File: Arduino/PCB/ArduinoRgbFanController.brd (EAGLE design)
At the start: 100 x 100 mm, 58 parts, among them IC2 ARDUINO_MKRFOX1200PROTOPADS, Q1 IRLML9301TRPBF, Q2 2N7002, Q3 2N7002, Q4 IRLML9301TRPBF

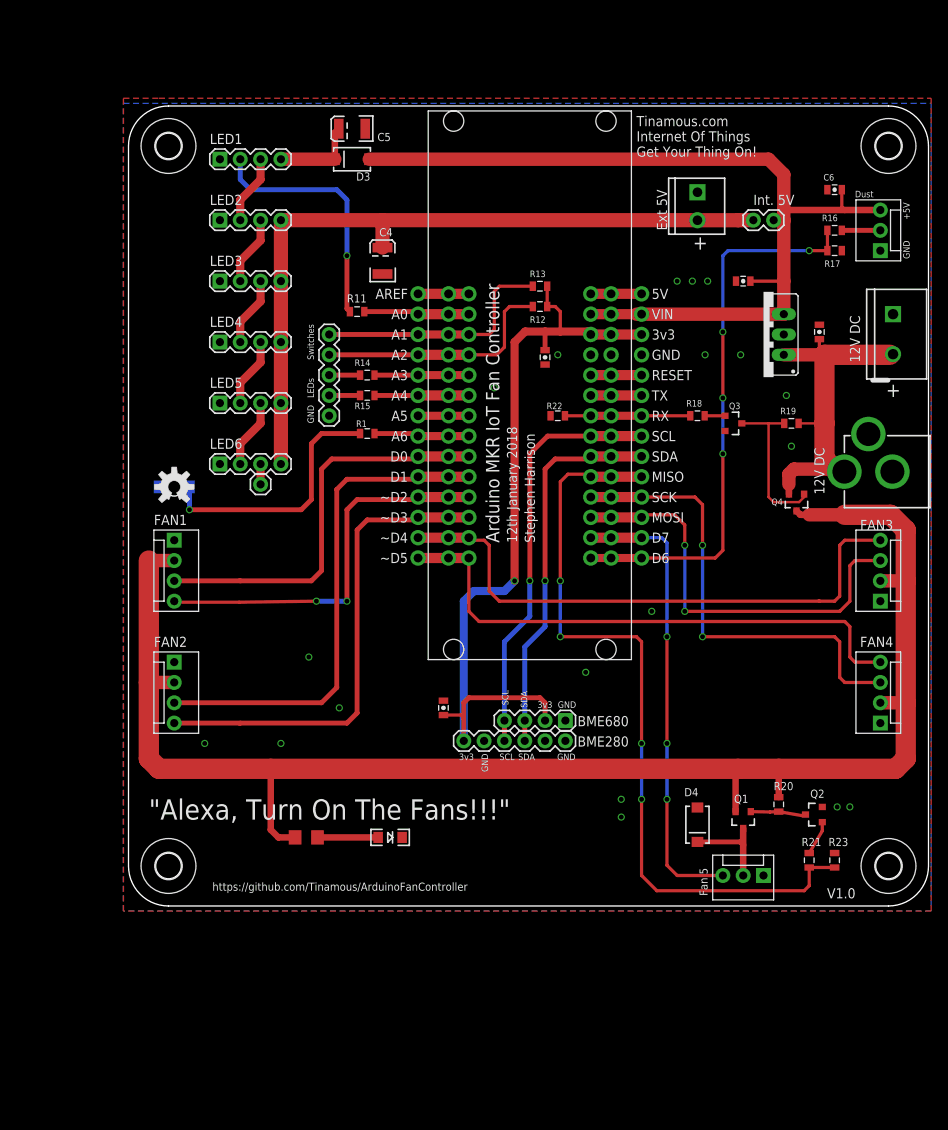
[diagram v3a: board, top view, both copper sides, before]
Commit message: Added 12v sense to detect low voltage and supply switched on.
Moved Fan5 connector up to leave a nice space at the bottom for the "Alexa..." thing.
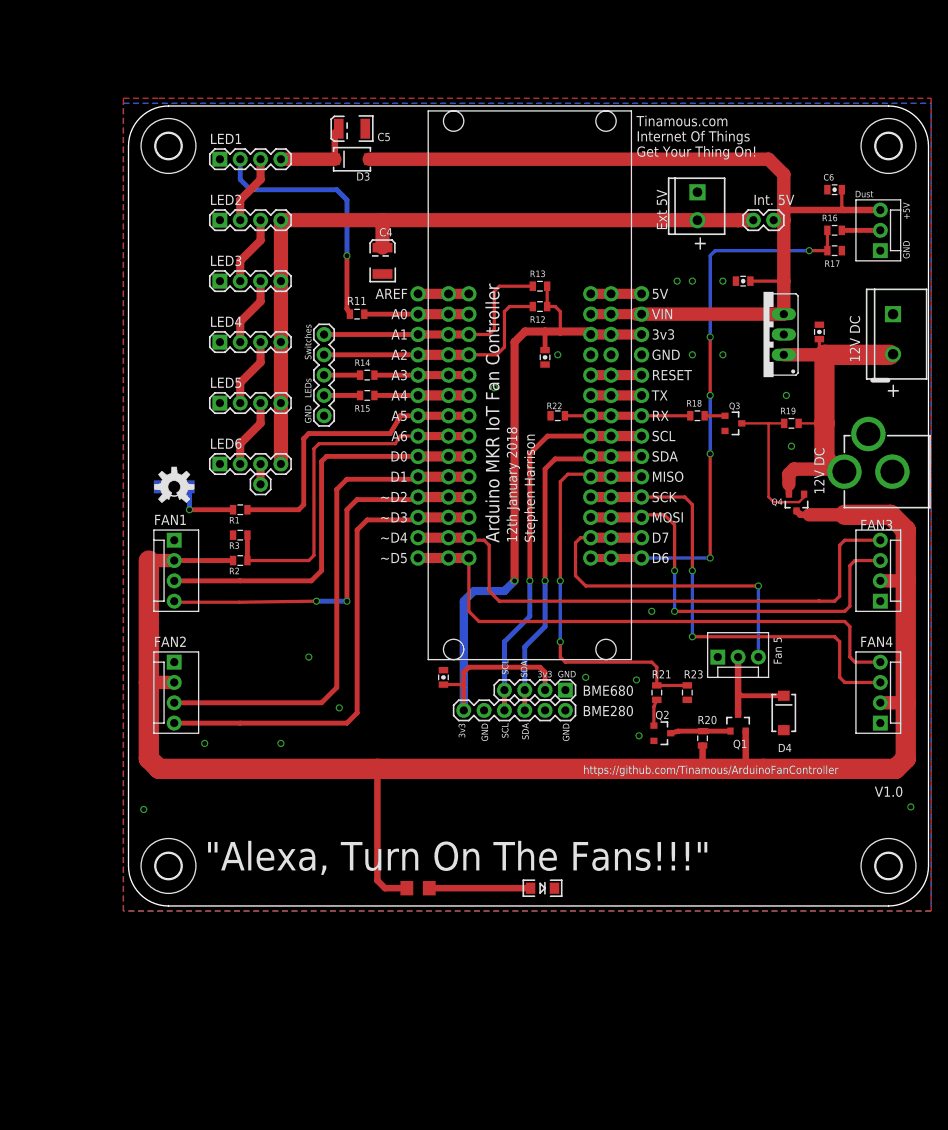
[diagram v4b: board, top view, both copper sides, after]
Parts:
- added R2: 40k, SparkFun-Resistors:0805
- added R3: 10k, SparkFun-Resistors:0805
- moved R21 28.3 mm to (66.0, 26.7), turned to 90 degrees
- moved R23 27.9 mm to (69.8, 26.7), turned to 270 degrees
- moved JP35 27.9 mm to (73.7, 31.1), turned to 0 degrees
- moved Q2 21.6 mm to (66.7, 21.6), turned to 270 degrees
- moved D2 20.1 mm to (51.8, 2.22)
- moved R1 18.5 mm to (14.0, 49.5)
- moved D4 17.7 mm to (81.9, 24.1), turned to 90 degrees
- moved R28 15.3 mm to (36.2, 2.22)
- moved R20 12.6 mm to (71.8, 21.0), turned to 270 degrees
- moved Q1 12.1 mm to (76.2, 22.9), turned to 0 degrees
- moved BME280 3.81 mm to (41.9, 24.4)
- moved BME680 3.81 mm to (54.6, 27.0)
- moved C7 3.81 mm to (39.4, 28.6)
- moved JP3 0.63 mm to (24.4, 61.3)
- moved R11 0.32 mm to (28.6, 74.0)
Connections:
- removed net SWITCH_ENABLED: IC2.#A5, IC2.@A5, IC2.A5
- new net FAN_POWER_SENSE: IC2.#A6, IC2.@A6, IC2.A6, R2.2, R3.1
- net FAN_POWER: now also R2.1
- net GND: now also R3.2
- net OSH_LED: now also IC2.#A5, IC2.@A5, IC2.A5; no longer IC2.#A6, IC2.@A6, IC2.A6
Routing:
- net FAN5_PWM: track 97.1 -> 51.3 mm, vias 4 -> 2
- net FAN_POWER_SENSE: track 0.00 -> 45.2 mm
- net OSH_LED: track 11.9 -> 37.7 mm
- net N$1: track 32.3 -> 8.35 mm
- net FAN_POWER: track 196.4 -> 211.3 mm
- net FAN5_TACH: track 57.6 -> 44.9 mm, vias 3 -> 1
- net SWITCH_ENABLED: track 6.35 -> 0.00 mm
- net N$94: track 7.58 -> 12.7 mm
- net SDA: track 47.7 -> 43.9 mm
- net SCL: track 52.1 -> 48.3 mm
- net 3.3V: track 101.4 -> 97.6 mm
- net N$28: track 6.90 -> 10.4 mm
- net N$12: track 11.8 -> 13.0 mm
- net N$32: track 4.31 -> 3.30 mm
- net SWITCH2: track 30.7 -> 31.4 mm
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
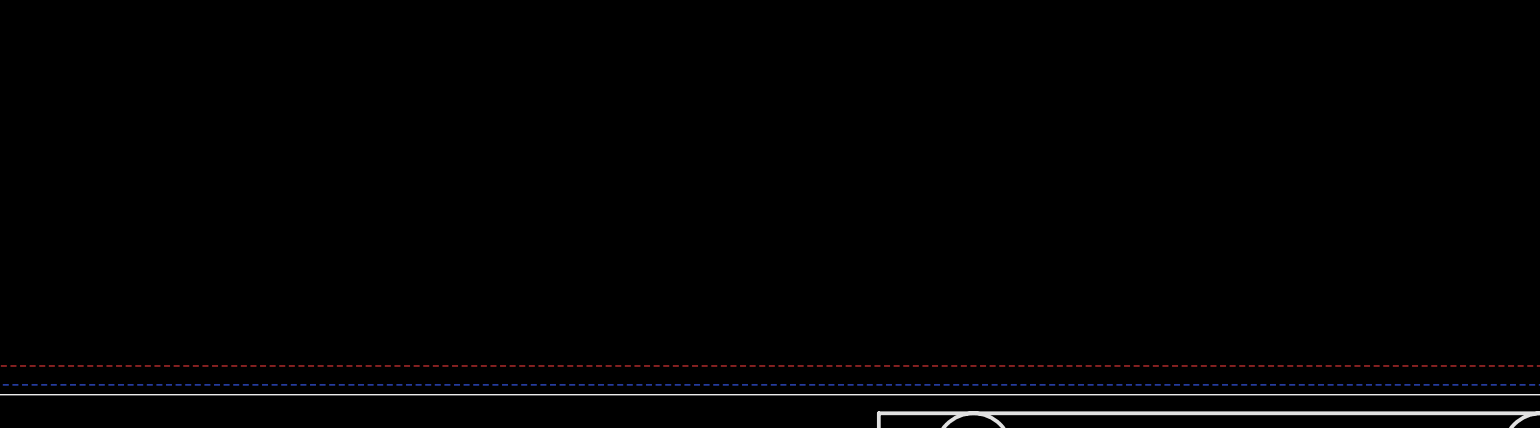
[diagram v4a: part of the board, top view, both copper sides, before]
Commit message: Added some value for components and some notes and dimensions for the PCB.
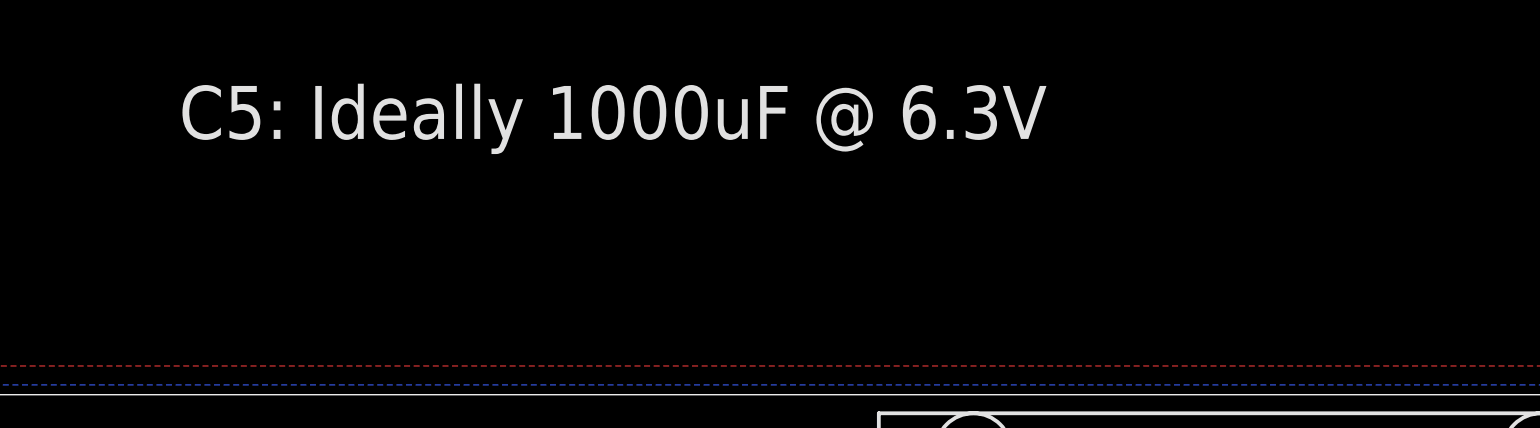
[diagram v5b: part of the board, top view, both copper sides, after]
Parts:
- R11: value (none) -> 470R
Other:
- board text added: "C5: Ideally 1000uF @ 6.3V"
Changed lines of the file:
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@@
 <setting verticaltext="up"/>
 </settings>
-<grid distance="0.025" unitdist="inch" unit="inch" style="lines" multiple="1" display="no" altdistance="0.0125" altunitdist="inch" altunit="inch"/>
+<grid distance="0.1" unitdist="mm" unit="mm" style="lines" multiple="1" display="no" altdistance="0.0125" altunitdist="inch" altunit="inch"/>
 <layers>
 <layer number="1" name="Top" color="4" fill="1" visible="yes" active="yes"/>
@@
 <text x="90.17" y="4.445" size="3.556" layer="26" ratio="15" rot="MR0">"Alexa, Turn On The Fans!!!"</text>
 <text x="72.39" y="83.82" size="1.778" layer="25" font="vector" ratio="10" rot="R180">+</text>
+<dimension x1="95" y1="0" x2="93.98" y2="25.4" x3="108.585" y3="12.7" textsize="1.778" layer="20" dtype="vertical"/>
+<dimension x1="95" y1="0" x2="93.98" y2="40.64" x3="114.3" y3="20.32" textsize="1.778" layer="20" dtype="vertical"/>
+<dimension x1="95" y1="0" x2="103.1875" y2="54.2925" x3="119.38" y3="27.14625" textsize="1.778" layer="20" dtype="vertical"/>
+<dimension x1="95" y1="0" x2="97.155" y2="69.85" x3="127" y3="34.925" textsize="1.778" layer="20" dtype="vertical"/>
+<dimension x1="94.9325" y1="65.7225" x2="96.52" y2="77.47" x3="111.125" y3="71.59625" textsize="1.778" layer="20" dtype="vertical"/>
+<dimension x1="95" y1="0" x2="60.325" y2="61.2775" x3="123.19" y3="30.63875" textsize="1.778" layer="20" dtype="vertical"/>
+<text x="13.97" y="108.585" size="1.778" layer="25">C5: Ideally 1000uF @ 6.3V</text>
+<dimension x1="93.98" y1="81.915" x2="95.25" y2="0" x3="135.89" y3="40.9575" textsize="1.778" layer="47" dtype="vertical"/>
+<dimension x1="40.005" y1="76.5175" x2="5" y2="95" x3="-6.5" y3="85.75875" textsize="1.778" layer="47" dtype="vertical"/>
+<dimension x1="40.005" y1="76.5175" x2="40.4" y2="100" x3="-11.2" y3="88.25875" textsize="1.778" layer="47" dtype="vertical"/>
+<dimension x1="40.005" y1="76.5175" x2="0" y2="74.1" x3="20.0025" y3="114.1" textsize="1.778" layer="47" dtype="horizontal"/>
 </plain>
 <attributes>
@@
 <attribute name="VALUE" x="13.335" y="53.975" size="1.27" layer="27" rot="R270"/>
 </element>
-<element name="R11" library="SparkFun-Resistors" package="0805" value="" x="28.575" y="73.9775" smashed="yes">
+<element name="R11" library="SparkFun-Resistors" package="0805" value="470R" x="28.575" y="73.9775" smashed="yes">
 <attribute name="NAME" x="27.305" y="75.1205" size="1.016" layer="25"/>
 <attribute name="VALUE" x="27.178" y="72.4535" size="0.4064" layer="27"/>
@@
 <attribute name="NAME" x="31.115" y="95.615" size="1.016" layer="25"/>
 <attribute name="VALUE" x="28.64" y="95.15" size="1.27" layer="27" rot="R90"/>
+<attribute name="FARNELL" value="1135048" x="27.94" y="97.155" size="1.778" layer="27" rot="R180" display="off"/>
 </element>
 <element name="BME280" library="SparkFun-Connectors" package="1X06" value="eBay BME280" x="41.91" y="24.4475" smashed="yes">

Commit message: Updated component values whilst building boards.
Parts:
- C1, C2, C7: value (none) -> 0.1uF
- C3: value (none) -> 1uF
- Q1, Q4: value IRLML9301TRPBF -> IRLML930
- R1: value (none) -> 1k
- R2: value 40k -> 43k
- R28: value 300R -> 1k
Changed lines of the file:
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@@
 <text x="90.17" y="4.445" size="3.556" layer="26" ratio="15" rot="MR0">"Alexa, Turn On The Fans!!!"</text>
 <text x="72.39" y="83.82" size="1.778" layer="25" font="vector" ratio="10" rot="R180">+</text>
-<dimension x1="95" y1="0" x2="93.98" y2="25.4" x3="108.585" y3="12.7" textsize="1.778" layer="20" dtype="vertical"/>
-<dimension x1="95" y1="0" x2="93.98" y2="40.64" x3="114.3" y3="20.32" textsize="1.778" layer="20" dtype="vertical"/>
-<dimension x1="95" y1="0" x2="103.1875" y2="54.2925" x3="119.38" y3="27.14625" textsize="1.778" layer="20" dtype="vertical"/>
-<dimension x1="95" y1="0" x2="97.155" y2="69.85" x3="127" y3="34.925" textsize="1.778" layer="20" dtype="vertical"/>
-<dimension x1="94.9325" y1="65.7225" x2="96.52" y2="77.47" x3="111.125" y3="71.59625" textsize="1.778" layer="20" dtype="vertical"/>
-<dimension x1="95" y1="0" x2="60.325" y2="61.2775" x3="123.19" y3="30.63875" textsize="1.778" layer="20" dtype="vertical"/>
+<dimension x1="95" y1="0" x2="93.98" y2="25.4" x3="108.585" y3="12.7" textsize="1.778" layer="47" dtype="vertical"/>
+<dimension x1="95" y1="0" x2="93.98" y2="40.64" x3="114.3" y3="20.32" textsize="1.778" layer="47" dtype="vertical"/>
+<dimension x1="95" y1="0" x2="103.1875" y2="54.2925" x3="119.38" y3="27.14625" textsize="1.778" layer="47" dtype="vertical"/>
+<dimension x1="95" y1="0" x2="97.155" y2="69.85" x3="127" y3="34.925" textsize="1.778" layer="47" dtype="vertical"/>
+<dimension x1="94.9325" y1="65.7225" x2="96.52" y2="77.47" x3="111.125" y3="71.59625" textsize="1.778" layer="47" dtype="vertical"/>
+<dimension x1="95" y1="0" x2="60.325" y2="61.2775" x3="123.19" y3="30.63875" textsize="1.778" layer="47" dtype="vertical"/>
 <text x="13.97" y="108.585" size="1.778" layer="25">C5: Ideally 1000uF @ 6.3V</text>
 <dimension x1="93.98" y1="81.915" x2="95.25" y2="0" x3="135.89" y3="40.9575" textsize="1.778" layer="47" dtype="vertical"/>
@@
 </autorouter>
 <elements>
-<element name="C1" library="SparkFun-Capacitors" package="0805-CAP" value="" x="86.36" y="71.755" smashed="yes" rot="R90">
+<element name="C1" library="SparkFun-Capacitors" package="0805-CAP" value="0.1uF" x="86.36" y="71.755" smashed="yes" rot="R90">
 <attribute name="VALUE" x="87.757" y="70.739" size="0.4064" layer="27" rot="R90"/>
 </element>
-<element name="C2" library="SparkFun-Capacitors" package="0805-CAP" value="" x="76.835" y="78.105" smashed="yes" rot="R180">
+<element name="C2" library="SparkFun-Capacitors" package="0805-CAP" value="0.1uF" x="76.835" y="78.105" smashed="yes" rot="R180">
 <attribute name="VALUE" x="77.851" y="79.502" size="0.4064" layer="27" rot="R180"/>
 </element>
@@
 <attribute name="VALUE" x="8.255" y="49.8475" size="1.27" layer="28" rot="MR0"/>
 </element>
-<element name="R1" library="SparkFun-Resistors" package="0805" value="" x="13.97" y="49.53" smashed="yes">
+<element name="R1" library="SparkFun-Resistors" package="0805" value="1k" x="13.97" y="49.53" smashed="yes">
 <attribute name="NAME" x="12.573" y="47.8155" size="0.8128" layer="25"/>
 <attribute name="VALUE" x="12.954" y="48.133" size="0.4064" layer="27"/>
@@
 <attribute name="PROD_ID" value="CONN-08197" x="103.1875" y="54.2925" size="1.27" layer="27" font="vector" rot="R90" display="off"/>
 </element>
-<element name="C3" library="SparkFun-Capacitors" package="0805-CAP" value="" x="52.07" y="68.58" smashed="yes" rot="R270">
+<element name="C3" library="SparkFun-Capacitors" package="0805-CAP" value="1uF" x="52.07" y="68.58" smashed="yes" rot="R270">
 <attribute name="VALUE" x="50.673" y="69.596" size="0.4064" layer="27" rot="R270"/>
 </element>
 <element name="LOGO3" library="SparkFun-Aesthetics" package="OSHW-LOGO-M" value="OSHW-LOGOM" x="5.715" y="52.3875"/>
-<element name="C7" library="SparkFun-Capacitors" package="0805-CAP" value="" x="39.37" y="28.575" smashed="yes" rot="R90">
+<element name="C7" library="SparkFun-Capacitors" package="0805-CAP" value="0.1uF" x="39.37" y="28.575" smashed="yes" rot="R90">
 <attribute name="VALUE" x="40.767" y="27.559" size="0.4064" layer="27" rot="R90"/>
 </element>
 <element name="IC2" library="Arduino" package="ARDUINO_MKRFOX1200_PROTOPADS" value="ARDUINO_MKRFOX1200PROTOPADS" x="37.465" y="30.7975"/>
-<element name="R28" library="SparkFun-Resistors" package="1206" value="300R" x="36.195" y="2.2225" smashed="yes">
+<element name="R28" library="SparkFun-Resistors" package="1206" value="1k" x="36.195" y="2.2225" smashed="yes">
 <attribute name="VALUE" x="36.449" y="1.778" size="0.4064" layer="27" rot="R90"/>
 </element>
@@
 <attribute name="VALUE" x="51.689" y="-0.1905" size="1.016" layer="27"/>
 </element>
-<element name="JP6" library="SparkFun-Connectors" package="MOLEX-1X4" value="Fan1" x="5.715" y="45.72" smashed="yes" rot="R270"/>
+<element name="JP6" library="SparkFun-Connectors" package="MOLEX-1X4" value="Fan1" x="5.715" y="45.72" smashed="yes" rot="R270">
+<attribute name="FARNELL" value="2313705" x="5.715" y="45.72" size="1.778" layer="27" rot="R270" display="off"/>
+<attribute name="MOLEX" value="47053-1000" x="5.715" y="45.72" size="1.778" layer="27" rot="R270" display="off"/>
+</element>
 <element name="JP8" library="SparkFun-Connectors" package="MOLEX-1X4" value="Fan2" x="5.715" y="30.48" smashed="yes" rot="R270"/>
 <element name="JP9" library="SparkFun-Connectors" package="MOLEX-1X4" value="Fan3" x="93.98" y="38.1" smashed="yes" rot="R90"/>
@@
 <attribute name="VALUE" x="10.16" y="52.07" size="1.27" layer="27"/>
 </element>
-<element name="Q1" library="SparkFun-DiscreteSemi" package="SOT23-3" value="IRLML9301TRPBF" x="76.2" y="22.86" smashed="yes">
+<element name="Q1" library="SparkFun-DiscreteSemi" package="SOT23-3" value="IRLML930" x="76.2" y="22.86" smashed="yes">
 <attribute name="PROD_ID" value="TRANS-08285" x="76.2" y="22.86" size="1.778" layer="27" display="off"/>
 <attribute name="NAME" x="77.343" y="20.7645" size="1.016" layer="25" rot="R180"/>
+<attribute name="FARNELL" value="1831089" x="76.2" y="22.86" size="1.778" layer="27" display="off"/>
 </element>
 <element name="Q2" library="SparkFun-DiscreteSemi" package="SOT23-3" value="2N7002" x="66.675" y="21.59" smashed="yes" rot="R270">
 <attribute name="PROD_ID" value="TRAN-12988" x="66.675" y="21.59" size="1.778" layer="27" rot="R270" display="off"/>
 <attribute name="NAME" x="65.8495" y="23.368" size="1.016" layer="25"/>
+<attribute name="FARNELL" value="1510761" x="66.675" y="21.59" size="1.778" layer="27" rot="R270" display="off"/>
 </element>
 <element name="R20" library="SparkFun-Resistors" package="0805" value="100k" x="71.755" y="20.955" smashed="yes" rot="R270">
@@
 <attribute name="NAME" x="75.057" y="62.103" size="0.8128" layer="25"/>
 <attribute name="VALUE" x="75.3745" y="61.341" size="0.4064" layer="27" rot="R270"/>
+<attribute name="FARNELL" value="1510761" x="75.565" y="60.325" size="1.778" layer="27" rot="R270" display="off"/>
 </element>
 <element name="R18" library="SparkFun-Resistors" package="0805" value="10R" x="71.12" y="61.2775" smashed="yes" rot="R180">
@@
 <attribute name="VALUE" x="70.993" y="61.976" size="0.4064" layer="27" rot="R270"/>
 </element>
-<element name="Q4" library="SparkFun-DiscreteSemi" package="SOT23-3" value="IRLML9301TRPBF" x="83.5025" y="50.4825" smashed="yes" rot="R180">
+<element name="Q4" library="SparkFun-DiscreteSemi" package="SOT23-3" value="IRLML930" x="83.5025" y="50.4825" smashed="yes" rot="R180">
 <attribute name="PROD_ID" value="TRANS-08285" x="83.5025" y="50.4825" size="1.778" layer="27" rot="R180" display="off"/>
 <attribute name="NAME" x="81.788" y="50.927" size="0.8128" layer="25" rot="R180"/>
+<attribute name="FARNELL" value="1831089" x="83.5025" y="50.4825" size="1.778" layer="27" rot="R180" display="off"/>
 </element>
 <element name="R19" library="SparkFun-Resistors" package="0805" value="100k" x="82.8675" y="60.325" smashed="yes" rot="R180">
@@
 <attribute name="VALUE" x="89.281" y="90.932" size="0.4064" layer="27" rot="R180"/>
 </element>
-<element name="R2" library="SparkFun-Resistors" package="0805" value="40k" x="13.97" y="43.18" smashed="yes">
+<element name="R2" library="SparkFun-Resistors" package="0805" value="43k" x="13.97" y="43.18" smashed="yes">
 <attribute name="NAME" x="12.573" y="41.4655" size="0.8128" layer="25"/>
 <attribute name="VALUE" x="14.097" y="42.799" size="0.4064" layer="27" rot="R90"/>
